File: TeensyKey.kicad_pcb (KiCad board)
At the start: 2 copper layers, 4 parts, among them SW1 MX-with-LED, U1 Teensy3.2

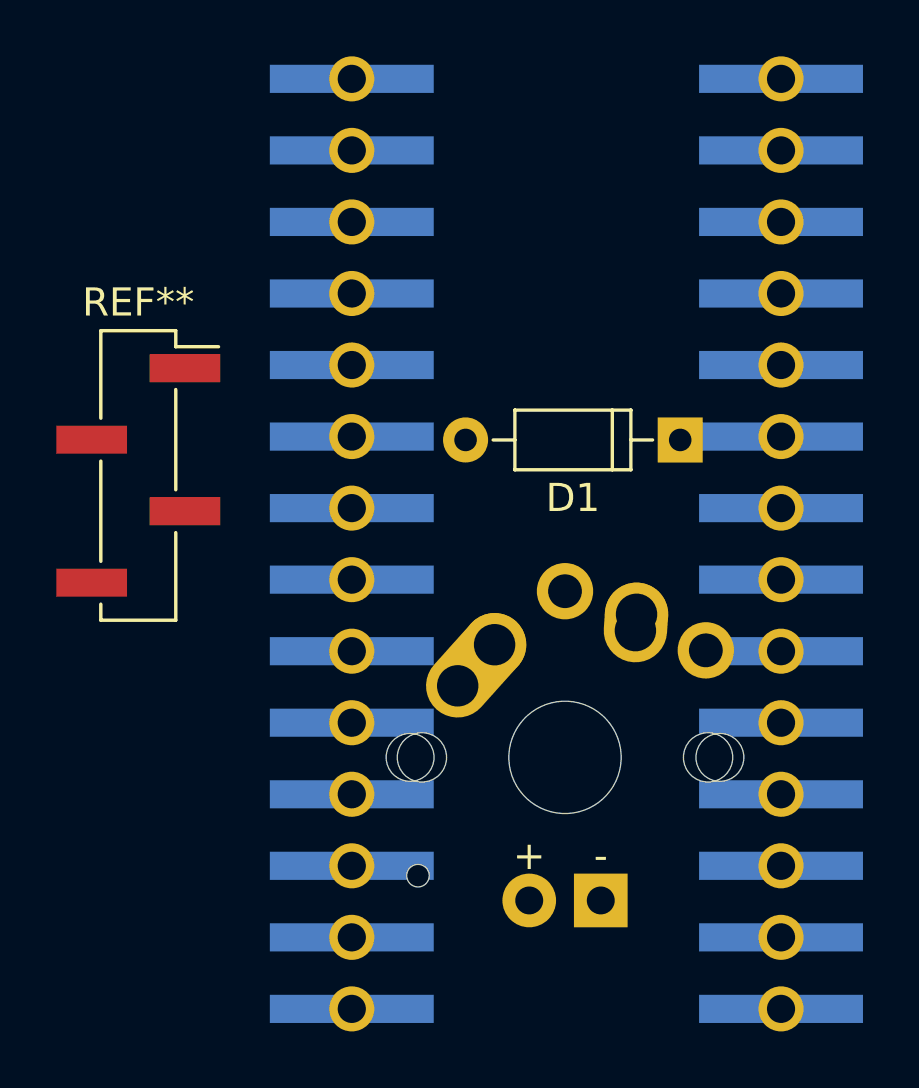
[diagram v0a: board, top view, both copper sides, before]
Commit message: laid out components
hid unused SMD pads
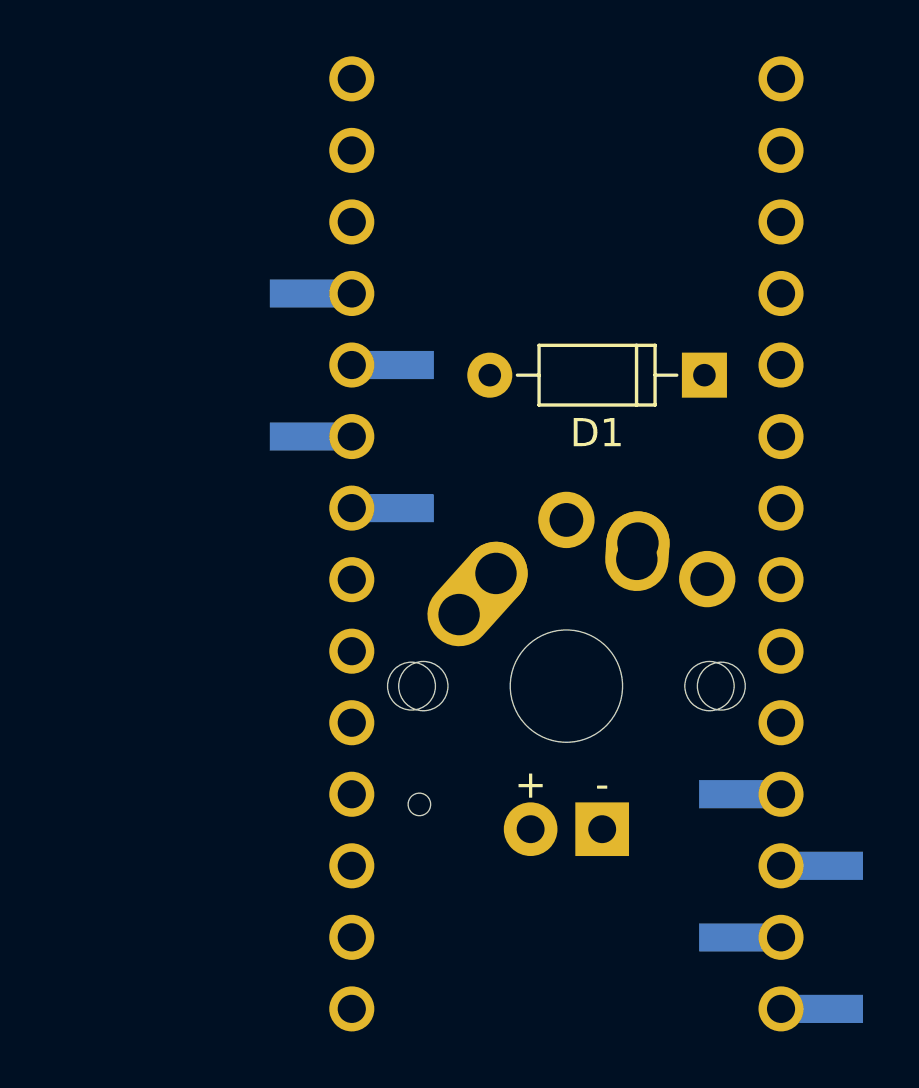
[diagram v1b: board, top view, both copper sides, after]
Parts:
- removed REF**: Pin_Header_Straight_1x04_Pitch2.54mm_SMD_Pin1Right, Pin_Headers:Pin_Header_Straight_1x04_Pitch2.54mm_SMD_Pin1Right
- moved SW1 2.53 mm to (142.8, 78.6)
- moved D1 2.46 mm to (147.7, 67.6)
